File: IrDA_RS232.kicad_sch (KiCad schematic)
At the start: 36 parts, among them J1 RS232, U1 MAX232, U2 MAX232, U3 MCP2155, U4 TFDU4301, Y1 11.0592 MHz

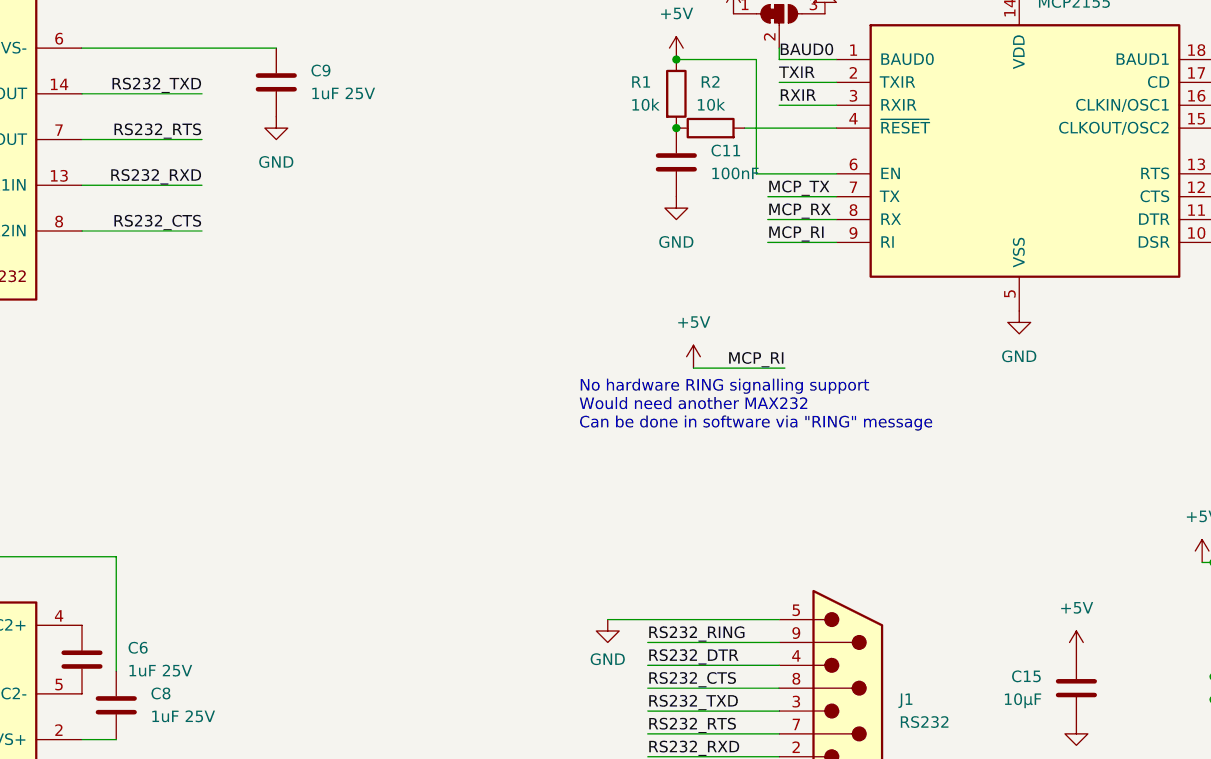
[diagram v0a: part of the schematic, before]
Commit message: schematic: add ring indication level converter
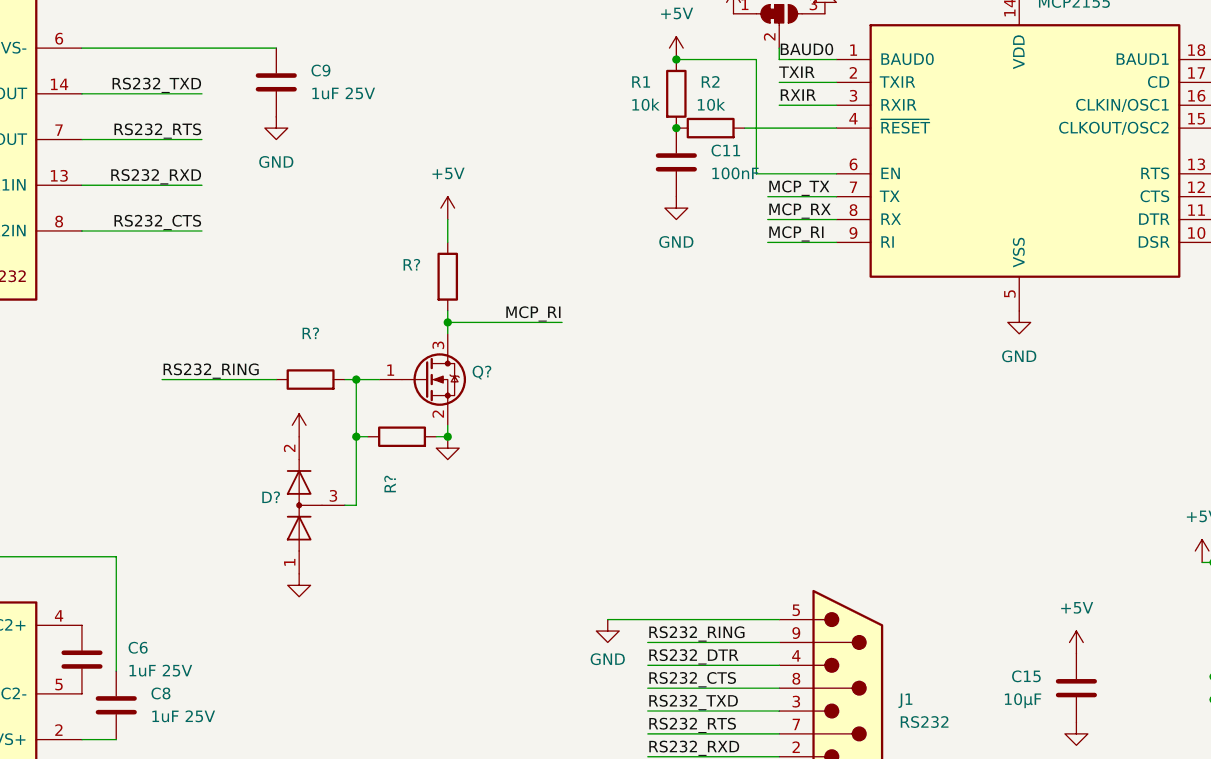
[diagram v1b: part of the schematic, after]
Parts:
- added D?: (no value), symbol Diode:BAV99
- added Q?: (no value), symbol Transistor_FET:2N7002
- added R? (x3): (no value), symbol Device:R
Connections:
- net +5V: now also D?.2 (A), R?.1; no longer U3.9 (RI)
- net GND: now also D?.1 (K), Q?.2 (S), R?.2
- net RS232_RING: now also R?.1
- new net: D?.3 (K), Q?.1 (G), R?.1, R?.2
- new net MCP_RI: Q?.3 (D), R?.2, U3.9 (RI)
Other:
- note removed: "No hardware RING signalling support Would need another MAX232 Can be done in software via "RING" message"

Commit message: add gerbers and PDF
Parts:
- D2: renamed from D?; value (none) -> BAV99; footprint (none) -> Package_TO_SOT_SMD:SOT-23
- Q1: renamed from Q?; value (none) -> 2N7002; footprint (none) -> Package_TO_SOT_SMD:SOT-23
- R7, R9: renamed from R?; value (none) -> 10k; footprint (none) -> Resistor_SMD:R_0402_1005Metric
- R8: renamed from R?; value (none) -> 100k; footprint (none) -> Resistor_SMD:R_0402_1005Metric
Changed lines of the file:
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@@
   (symbol (lib_id "Transistor_FET:2N7002") (at 124.46 87.63 0) (unit 1)
     (in_bom yes) (on_board yes) (fields_autoplaced)
-    (property "Reference" "Q?" (id 0) (at 129.667 86.7953 0)
-      (effects (font (size 1.27 1.27)) (justify left))
-    )
-    (property "Value" "" (id 1) (at 129.667 89.3322 0)
-      (effects (font (size 1.27 1.27)) (justify left))
-    )
-    (property "Footprint" "" (id 2) (at 129.54 89.535 0)
+    (property "Reference" "Q1" (id 0) (at 129.667 86.7953 0)
+      (effects (font (size 1.27 1.27)) (justify left))
+    )
+    (property "Value" "2N7002" (id 1) (at 129.667 89.3322 0)
+      (effects (font (size 1.27 1.27)) (justify left))
+    )
+    (property "Footprint" "Package_TO_SOT_SMD:SOT-23" (id 2) (at 129.54 89.535 0)
       (effects (font (size 1.27 1.27) italic) (justify left) hide)
     )
@@
   (symbol (lib_id "power:GND") (at 127 93.98 0) (unit 1)
     (in_bom yes) (on_board yes) (fields_autoplaced)
-    (property "Reference" "#PWR?" (id 0) (at 127 100.33 0)
-      (effects (font (size 1.27 1.27)) hide)
-    )
-    (property "Value" "" (id 1) (at 127 98.4234 0))
+    (property "Reference" "#PWR0135" (id 0) (at 127 100.33 0)
+      (effects (font (size 1.27 1.27)) hide)
+    )
+    (property "Value" "GND" (id 1) (at 127 98.4234 0))
     (property "Footprint" "" (id 2) (at 127 93.98 0)
       (effects (font (size 1.27 1.27)) hide)
@@
   (symbol (lib_id "Device:R") (at 111.76 87.63 90) (unit 1)
     (in_bom yes) (on_board yes)
-    (property "Reference" "R?" (id 0) (at 111.76 82.55 90))
-    (property "Value" "" (id 1) (at 111.76 85.09 90))
-    (property "Footprint" "" (id 2) (at 111.76 89.408 90)
+    (property "Reference" "R7" (id 0) (at 111.76 82.55 90))
+    (property "Value" "10k" (id 1) (at 111.76 85.09 90))
+    (property "Footprint" "Resistor_SMD:R_0402_1005Metric" (id 2) (at 111.76 89.408 90)
       (effects (font (size 1.27 1.27)) hide)
     )
@@
   (symbol (lib_id "power:GND") (at 110.49 109.22 0) (unit 1)
     (in_bom yes) (on_board yes) (fields_autoplaced)
-    (property "Reference" "#PWR?" (id 0) (at 110.49 115.57 0)
-      (effects (font (size 1.27 1.27)) hide)
-    )
-    (property "Value" "" (id 1) (at 110.49 113.6634 0))
+    (property "Reference" "#PWR0133" (id 0) (at 110.49 115.57 0)
+      (effects (font (size 1.27 1.27)) hide)
+    )
+    (property "Value" "GND" (id 1) (at 110.49 113.6634 0))
     (property "Footprint" "" (id 2) (at 110.49 109.22 0)
       (effects (font (size 1.27 1.27)) hide)
@@
   (symbol (lib_id "power:+5V") (at 110.49 93.98 0) (unit 1)
     (in_bom yes) (on_board yes) (fields_autoplaced)
-    (property "Reference" "#PWR?" (id 0) (at 110.49 97.79 0)
-      (effects (font (size 1.27 1.27)) hide)
-    )
-    (property "Value" "" (id 1) (at 110.49 90.4042 0))
+    (property "Reference" "#PWR0134" (id 0) (at 110.49 97.79 0)
+      (effects (font (size 1.27 1.27)) hide)
+    )
+    (property "Value" "+5V" (id 1) (at 110.49 90.4042 0))
     (property "Footprint" "" (id 2) (at 110.49 93.98 0)
       (effects (font (size 1.27 1.27)) hide)
@@
   (symbol (lib_id "Device:R") (at 127 76.2 0) (unit 1)
     (in_bom yes) (on_board yes)
-    (property "Reference" "R?" (id 0) (at 121.92 74.93 0)
-      (effects (font (size 1.27 1.27)) (justify left))
-    )
-    (property "Value" "" (id 1) (at 121.92 77.47 0)
-      (effects (font (size 1.27 1.27)) (justify left))
-    )
-    (property "Footprint" "" (id 2) (at 125.222 76.2 90)
+    (property "Reference" "R9" (id 0) (at 121.92 74.93 0)
+      (effects (font (size 1.27 1.27)) (justify left))
+    )
+    (property "Value" "10k" (id 1) (at 121.92 77.47 0)
+      (effects (font (size 1.27 1.27)) (justify left))
+    )
+    (property "Footprint" "Resistor_SMD:R_0402_1005Metric" (id 2) (at 125.222 76.2 90)
       (effects (font (size 1.27 1.27)) hide)
     )
@@
   (symbol (lib_id "Diode:BAV99") (at 110.49 101.6 90) (unit 1)
     (in_bom yes) (on_board yes) (fields_autoplaced)
-    (property "Reference" "D?" (id 0) (at 108.4834 100.7653 90)
-      (effects (font (size 1.27 1.27)) (justify left))
-    )
-    (property "Value" "" (id 1) (at 108.4834 103.3022 90)
-      (effects (font (size 1.27 1.27)) (justify left))
-    )
-    (property "Footprint" "" (id 2) (at 123.19 101.6 0)
+    (property "Reference" "D2" (id 0) (at 108.4834 100.7653 90)
+      (effects (font (size 1.27 1.27)) (justify left))
+    )
+    (property "Value" "BAV99" (id 1) (at 108.4834 103.3022 90)
+      (effects (font (size 1.27 1.27)) (justify left))
+    )
+    (property "Footprint" "Package_TO_SOT_SMD:SOT-23" (id 2) (at 123.19 101.6 0)
       (effects (font (size 1.27 1.27)) hide)
     )
@@
   (symbol (lib_id "Device:R") (at 121.92 93.98 90) (unit 1)
     (in_bom yes) (on_board yes)
-    (property "Reference" "R?" (id 0) (at 120.65 100.33 0)
-      (effects (font (size 1.27 1.27)) (justify left))
-    )
-    (property "Value" "" (id 1) (at 123.19 100.33 0)
-      (effects (font (size 1.27 1.27)) (justify left))
-    )
-    (property "Footprint" "" (id 2) (at 121.92 95.758 90)
+    (property "Reference" "R8" (id 0) (at 120.65 100.33 0)
+      (effects (font (size 1.27 1.27)) (justify left))
+    )
+    (property "Value" "100k" (id 1) (at 123.19 100.33 0)
+      (effects (font (size 1.27 1.27)) (justify left))
+    )
+    (property "Footprint" "Resistor_SMD:R_0402_1005Metric" (id 2) (at 121.92 95.758 90)
       (effects (font (size 1.27 1.27)) hide)
     )
@@
       (reference "#PWR0132") (unit 1) (value "GND") (footprint "")
     )
+    (path "/702f05a4-fae3-4f6c-99ae-b98c29fc4287"
+      (reference "#PWR0133") (unit 1) (value "GND") (footprint "")
+    )
+    (path "/74522d7f-1de2-43f7-a63b-c7cd8b82854a"
+      (reference "#PWR0134") (unit 1) (value "+5V") (footprint "")
+    )
     (path "/09e14f91-fe29-49d2-898b-f2d9b0e888bd"
-      (reference "#PWR?") (unit 1) (value "GND") (footprint "")
-    )
-    (path "/702f05a4-fae3-4f6c-99ae-b98c29fc4287"
-      (reference "#PWR?") (unit 1) (value "GND") (footprint "")
-    )
-    (path "/74522d7f-1de2-43f7-a63b-c7cd8b82854a"
-      (reference "#PWR?") (unit 1) (value "+5V") (footprint "")
+      (reference "#PWR0135") (unit 1) (value "GND") (footprint "")
     )
     (path "/0fe10355-9bff-451d-9553-0e09162ee625"
@@
     )
     (path "/a7259668-a7be-4c21-96a4-8846ac80b0fb"
-      (reference "D?") (unit 1) (value "BAV99") (footprint "Package_TO_SOT_SMD:SOT-23")
+      (reference "D2") (unit 1) (value "BAV99") (footprint "Package_TO_SOT_SMD:SOT-23")
     )
     (path "/ba033dd1-a5e2-4136-b71b-d0a1cef6fc1f"
@@
     )
     (path "/078e5fce-dc80-42bb-9ac4-ed74a2790404"
-      (reference "Q?") (unit 1) (value "2N7002") (footprint "Package_TO_SOT_SMD:SOT-23")
+      (reference "Q1") (unit 1) (value "2N7002") (footprint "Package_TO_SOT_SMD:SOT-23")
     )
     (path "/b5a0fbce-d141-4b97-bbb7-f5d9c46936d1"
@@
     )
     (path "/530a98c5-6c9e-4c5a-a886-92ee0aae938c"
-      (reference "R?") (unit 1) (value "10k") (footprint "Resistor_SMD:R_0402_1005Metric")
+      (reference "R7") (unit 1) (value "10k") (footprint "Resistor_SMD:R_0402_1005Metric")
+    )
+    (path "/c378b76e-6761-4295-9491-256a4807b525"
+      (reference "R8") (unit 1) (value "100k") (footprint "Resistor_SMD:R_0402_1005Metric")
     )
     (path "/7fb75c5d-91f3-4b8a-b65f-96e16520f644"
-      (reference "R?") (unit 1) (value "10k") (footprint "Resistor_SMD:R_0402_1005Metric")
-    )
-    (path "/c378b76e-6761-4295-9491-256a4807b525"
-      (reference "R?") (unit 1) (value "100k") (footprint "Resistor_SMD:R_0402_1005Metric")
+      (reference "R9") (unit 1) (value "10k") (footprint "Resistor_SMD:R_0402_1005Metric")
     )
     (path "/fff239a0-819c-422a-8274-b2a8a4670a45"
